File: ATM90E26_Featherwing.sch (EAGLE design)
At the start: 56 parts, among them J1 ST-PJ-312, J2 4P-SMD-2.0-90D, J3 4P-SMD-2.0-90D, J4 12V AC, Q1 8.192MHz, U1 ATM90E26, U2 CJT1117-5.0-SOT223

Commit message: Applied hackvana DRU
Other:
- note added: "Grove Connectors"
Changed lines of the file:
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@@
 <?xml version="1.0" encoding="utf-8"?>
 <!DOCTYPE eagle SYSTEM "eagle.dtd">
-<eagle version="7.4.0">
+<eagle version="7.6.0">
 <drawing>
 <settings>
@@
 <grid distance="0.1" unitdist="inch" unit="inch" style="lines" multiple="1" display="no" altdistance="0.01" altunitdist="inch" altunit="inch"/>
 <layers>
-<layer number="1" name="Top" color="4" fill="1" visible="yes" active="no"/>
-<layer number="16" name="Bottom" color="1" fill="1" visible="yes" active="no"/>
-<layer number="17" name="Pads" color="2" fill="1" visible="yes" active="no"/>
-<layer number="18" name="Vias" color="2" fill="1" visible="yes" active="no"/>
-<layer number="19" name="Unrouted" color="6" fill="1" visible="yes" active="no"/>
-<layer number="20" name="Dimension" color="15" fill="1" visible="yes" active="no"/>
-<layer number="21" name="tPlace" color="7" fill="1" visible="yes" active="no"/>
-<layer number="22" name="bPlace" color="13" fill="1" visible="yes" active="no"/>
-<layer number="23" name="tOrigins" color="15" fill="1" visible="yes" active="no"/>
-<layer number="24" name="bOrigins" color="15" fill="1" visible="yes" active="no"/>
-<layer number="25" name="tNames" color="7" fill="1" visible="yes" active="no"/>
-<layer number="26" name="bNames" color="13" fill="1" visible="yes" active="no"/>
-<layer number="27" name="tValues" color="7" fill="1" visible="yes" active="no"/>
-<layer number="28" name="bValues" color="7" fill="1" visible="yes" active="no"/>
+<layer number="1" name="Top" color="4" fill="1" visible="no" active="no"/>
+<layer number="16" name="Bottom" color="1" fill="1" visible="no" active="no"/>
+<layer number="17" name="Pads" color="2" fill="1" visible="no" active="no"/>
+<layer number="18" name="Vias" color="2" fill="1" visible="no" active="no"/>
+<layer number="19" name="Unrouted" color="6" fill="1" visible="no" active="no"/>
+<layer number="20" name="Dimension" color="15" fill="1" visible="no" active="no"/>
+<layer number="21" name="tPlace" color="7" fill="1" visible="no" active="no"/>
+<layer number="22" name="bPlace" color="13" fill="1" visible="no" active="no"/>
+<layer number="23" name="tOrigins" color="15" fill="1" visible="no" active="no"/>
+<layer number="24" name="bOrigins" color="15" fill="1" visible="no" active="no"/>
+<layer number="25" name="tNames" color="7" fill="1" visible="no" active="no"/>
+<layer number="26" name="bNames" color="13" fill="1" visible="no" active="no"/>
+<layer number="27" name="tValues" color="7" fill="1" visible="no" active="no"/>
+<layer number="28" name="bValues" color="7" fill="1" visible="no" active="no"/>
 <layer number="29" name="tStop" color="7" fill="3" visible="no" active="no"/>
 <layer number="30" name="bStop" color="7" fill="6" visible="no" active="no"/>
@@
 <layer number="35" name="tGlue" color="7" fill="4" visible="no" active="no"/>
 <layer number="36" name="bGlue" color="7" fill="5" visible="no" active="no"/>
-<layer number="37" name="tTest" color="7" fill="1" visible="yes" active="no"/>
-<layer number="38" name="bTest" color="7" fill="1" visible="yes" active="no"/>
+<layer number="37" name="tTest" color="7" fill="1" visible="no" active="no"/>
+<layer number="38" name="bTest" color="7" fill="1" visible="no" active="no"/>
 <layer number="39" name="tKeepout" color="4" fill="11" visible="no" active="no"/>
 <layer number="40" name="bKeepout" color="1" fill="11" visible="no" active="no"/>
@@
 <layer number="44" name="Drills" color="7" fill="1" visible="no" active="no"/>
 <layer number="45" name="Holes" color="7" fill="1" visible="no" active="no"/>
-<layer number="46" name="Milling" color="3" fill="1" visible="yes" active="no"/>
-<layer number="47" name="Measures" color="7" fill="1" visible="yes" active="no"/>
-<layer number="48" name="Document" color="7" fill="1" visible="yes" active="no"/>
-<layer number="49" name="Reference" color="7" fill="1" visible="yes" active="no"/>
-<layer number="50" name="dxf" color="7" fill="1" visible="yes" active="no"/>
-<layer number="51" name="tDocu" color="7" fill="1" visible="yes" active="no"/>
-<layer number="52" name="bDocu" color="7" fill="1" visible="yes" active="no"/>
-<layer number="53" name="tGND_GNDA" color="7" fill="9" visible="yes" active="no"/>
-<layer number="54" name="bGND_GNDA" color="1" fill="9" visible="yes" active="no"/>
-<layer number="56" name="wert" color="7" fill="1" visible="yes" active="no"/>
-<layer number="57" name="tCAD" color="7" fill="1" visible="yes" active="no"/>
-<layer number="59" name="tCarbon" color="7" fill="1" visible="yes" active="no"/>
-<layer number="60" name="bCarbon" color="7" fill="1" visible="yes" active="no"/>
+<layer number="46" name="Milling" color="3" fill="1" visible="no" active="no"/>
+<layer number="47" name="Measures" color="7" fill="1" visible="no" active="no"/>
+<layer number="48" name="Document" color="7" fill="1" visible="no" active="no"/>
+<layer number="49" name="Reference" color="7" fill="1" visible="no" active="no"/>
+<layer number="50" name="dxf" color="7" fill="1" visible="no" active="no"/>
+<layer number="51" name="tDocu" color="7" fill="1" visible="no" active="no"/>
+<layer number="52" name="bDocu" color="7" fill="1" visible="no" active="no"/>
+<layer number="53" name="tGND_GNDA" color="7" fill="9" visible="no" active="no"/>
+<layer number="54" name="bGND_GNDA" color="1" fill="9" visible="no" active="no"/>
+<layer number="56" name="wert" color="7" fill="1" visible="no" active="no"/>
+<layer number="57" name="tCAD" color="7" fill="1" visible="no" active="no"/>
+<layer number="59" name="tCarbon" color="7" fill="1" visible="no" active="no"/>
+<layer number="60" name="bCarbon" color="7" fill="1" visible="no" active="no"/>
 <layer number="90" name="Modules" color="5" fill="1" visible="yes" active="yes"/>
 <layer number="91" name="Nets" color="2" fill="1" visible="yes" active="yes"/>
@@
 <wire x1="101.6" y1="22.86" x2="101.6" y2="-76.2" width="0.1524" layer="94"/>
 <text x="0" y="17.78" size="2.54" layer="94">Voltage and Current Sampling + Supply</text>
+<text x="142.24" y="-22.86" size="2.54" layer="94">Grove Connectors</text>
 </plain>
 <instances>

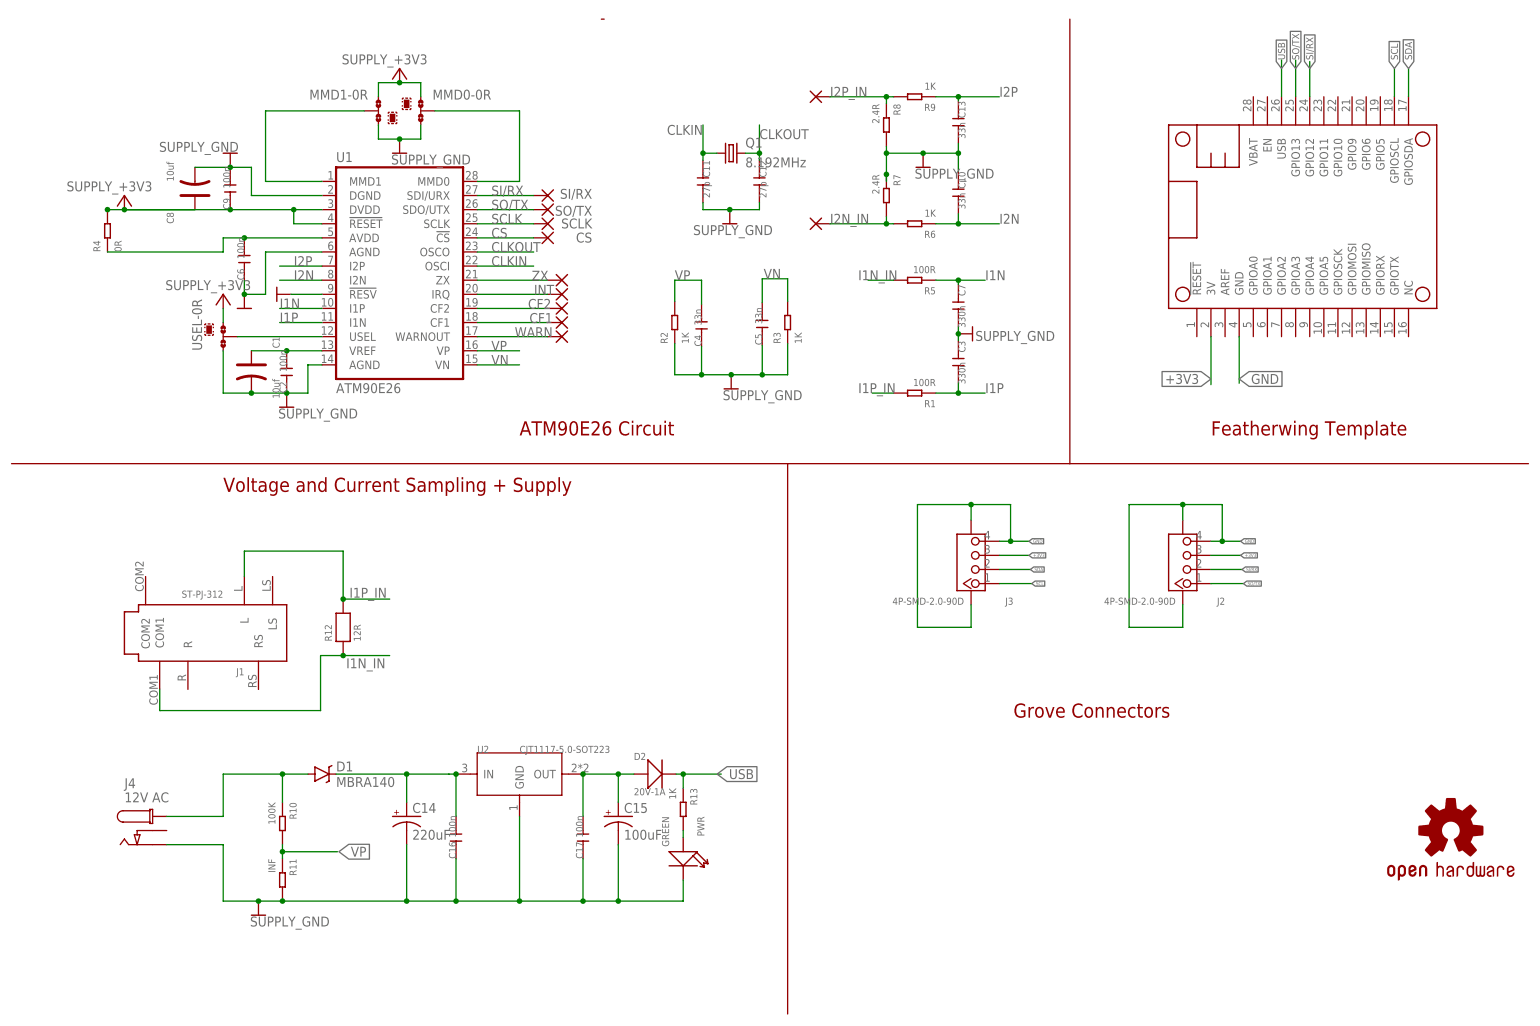
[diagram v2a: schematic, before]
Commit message: Ass spi/uart mux pins
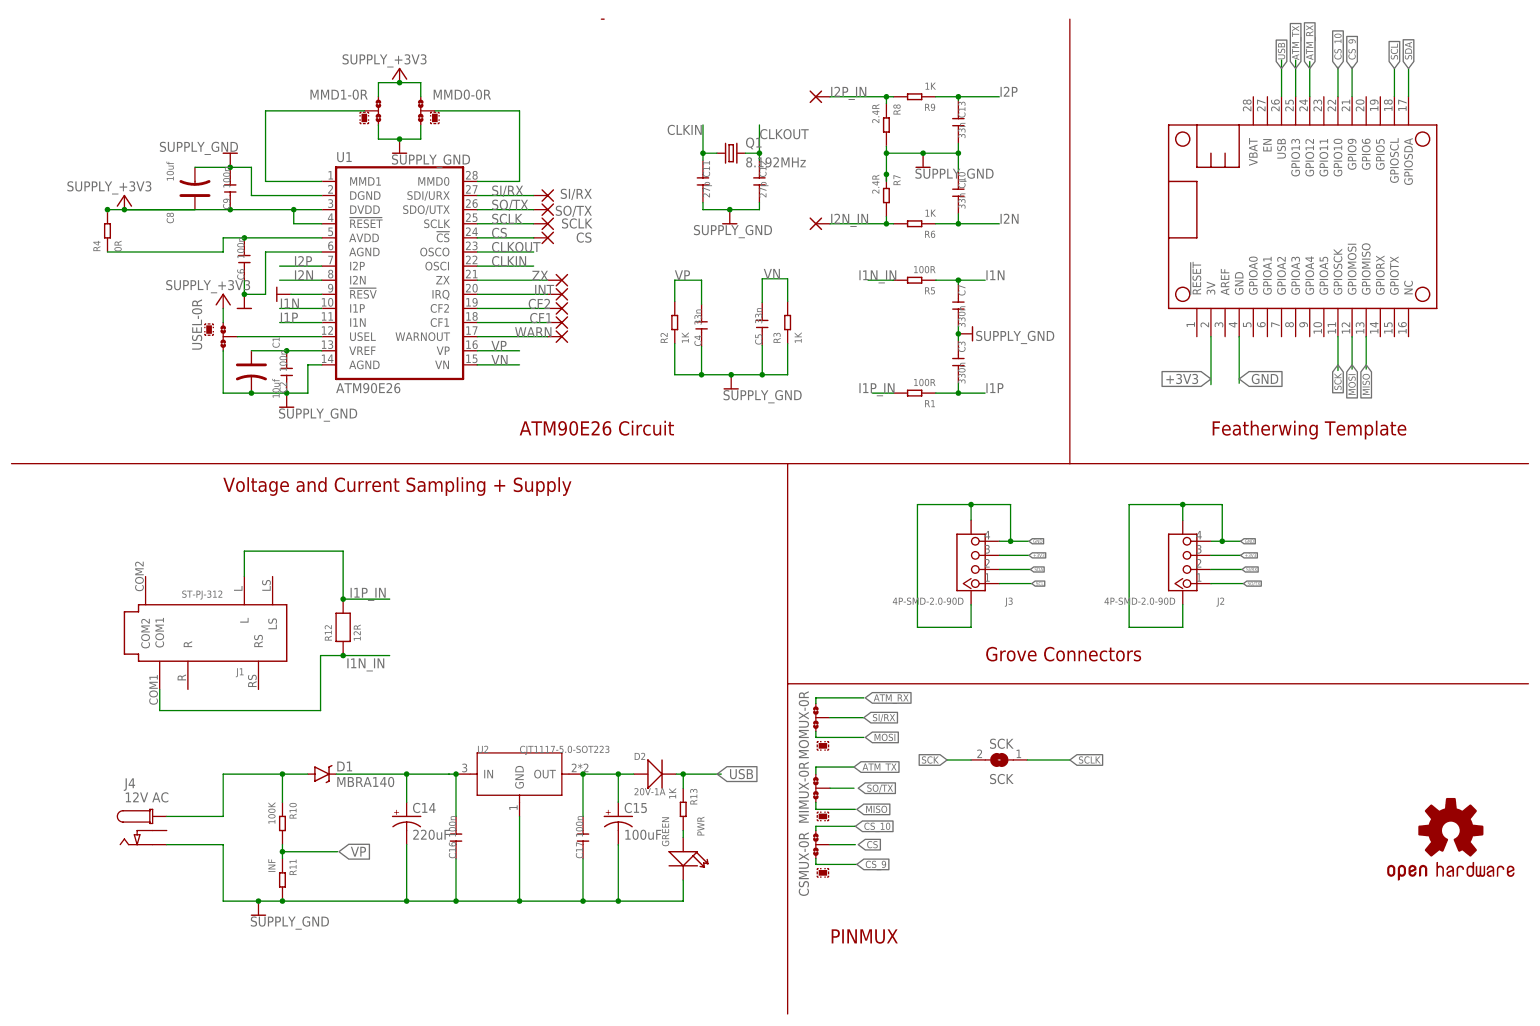
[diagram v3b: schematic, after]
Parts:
- added CSMUX, MIMUX, MOMUX: 0R-JUMPA, jump-0r-smd:0R-JUMPA
- added SCK: SCK, jumper:SJ
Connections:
- new net ATM_RX: MOMUX-0R.1, MS1.GPIO12
- new net ATM_TX: MIMUX-0R.1, MS1.GPIO13
- new net CS_10: CSMUX-0R.1, MS1.GPIO10
- new net CS_9: CSMUX-0R.3, MS1.GPIO9
- new net MISO: MIMUX-0R.3, MS1.GPIOMISO
- new net MOSI: MOMUX-0R.3, MS1.GPIOMOSI
- new net SCK: MS1.GPIOSCK, SCK.2
- net CS: now also CSMUX-0R.2
- net SCLK: now also SCK.1
- net SI/RX: now also MOMUX-0R.2; no longer MS1.GPIO12
- net SO/TX: now also MIMUX-0R.2; no longer MS1.GPIO13
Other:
- note added: "PINMUX"
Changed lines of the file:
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@@
 <?xml version="1.0" encoding="utf-8"?>
 <!DOCTYPE eagle SYSTEM "eagle.dtd">
-<eagle version="7.6.0">
+<eagle version="7.4.0">
 <drawing>
 <settings>
@@
 <layers>
 <layer number="1" name="Top" color="4" fill="1" visible="no" active="no"/>
+<layer number="2" name="Route2" color="1" fill="3" visible="no" active="no"/>
+<layer number="15" name="Route15" color="4" fill="6" visible="no" active="no"/>
 <layer number="16" name="Bottom" color="1" fill="1" visible="no" active="no"/>
 <layer number="17" name="Pads" color="2" fill="1" visible="no" active="no"/>
@@
 <part name="C16" library="Discrete" deviceset="C*" device="-0603" value="100n"/>
 <part name="C17" library="Discrete" deviceset="C*" device="-0603" value="100n"/>
+<part name="MOMUX" library="jump-0r-smd" deviceset="0R-JUMP" device="A" value="0R-JUMPA"/>
+<part name="MIMUX" library="jump-0r-smd" deviceset="0R-JUMP" device="A" value="0R-JUMPA"/>
+<part name="CSMUX" library="jump-0r-smd" deviceset="0R-JUMP" device="A" value="0R-JUMPA"/>
+<part name="SCK" library="jumper" deviceset="SJ" device="" value="SCK"/>
 </parts>
 <sheets>
@@
 <text x="53.34" y="27.94" size="2.54" layer="94" ratio="20">ATM90E26 Circuit</text>
 <text x="177.8" y="27.94" size="2.54" layer="94" ratio="20">Featherwing Template</text>
-<wire x1="101.6" y1="22.86" x2="101.6" y2="-76.2" width="0.1524" layer="94"/>
+<wire x1="101.6" y1="22.86" x2="101.6" y2="-16.764" width="0.1524" layer="94"/>
 <text x="0" y="17.78" size="2.54" layer="94">Voltage and Current Sampling + Supply</text>
-<text x="142.24" y="-22.86" size="2.54" layer="94">Grove Connectors</text>
+<text x="137.16" y="-12.7" size="2.54" layer="94">Grove Connectors</text>
+<wire x1="101.6" y1="-16.764" x2="101.6" y2="-76.2" width="0.1524" layer="94"/>
+<wire x1="101.6" y1="-16.764" x2="234.95" y2="-16.764" width="0.1524" layer="94"/>
+<text x="109.22" y="-63.5" size="2.54" layer="94">PINMUX</text>
 </plain>
 <instances>
@@
 <attribute name="NAME" x="15.494" y="88.392" size="1.778" layer="95"/>
 </instance>
-<instance part="MMD1" gate="G$2" x="30.48" y="83.82" rot="R180"/>
+<instance part="MMD1" gate="G$2" x="25.4" y="83.82" rot="R180"/>
 <instance part="MMD0" gate="-0R" x="35.56" y="86.36" smashed="yes">
 <attribute name="NAME" x="48.26" y="90.17" size="1.778" layer="95" rot="R180"/>
 </instance>
-<instance part="MMD0" gate="G$2" x="33.02" y="88.9"/>
+<instance part="MMD0" gate="G$2" x="38.1" y="83.82" rot="R180"/>
 <instance part="+3V3" gate="G$1" x="31.75" y="91.44" smashed="yes">
 <attribute name="VALUE" x="21.336" y="94.742" size="1.778" layer="96"/>
@@
 <instance part="C16" gate="C" x="41.91" y="-44.45" rot="R90"/>
 <instance part="C17" gate="C" x="64.77" y="-44.45" rot="R90"/>
+<instance part="MOMUX" gate="-0R" x="106.68" y="-22.86" smashed="yes">
+<attribute name="NAME" x="103.632" y="-18.034" size="1.778" layer="95" rot="R270"/>
+</instance>
+<instance part="MOMUX" gate="G$2" x="109.22" y="-27.94" rot="R270"/>
+<instance part="MIMUX" gate="-0R" x="106.68" y="-35.56" smashed="yes">
+<attribute name="NAME" x="103.632" y="-30.734" size="1.778" layer="95" rot="R270"/>
+</instance>
+<instance part="MIMUX" gate="G$2" x="109.22" y="-40.64" rot="R270"/>
+<instance part="CSMUX" gate="-0R" x="106.68" y="-45.72" smashed="yes">
+<attribute name="NAME" x="103.632" y="-43.434" size="1.778" layer="95" rot="R270"/>
+</instance>
+<instance part="CSMUX" gate="G$2" x="109.22" y="-50.8" rot="R270"/>
+<instance part="SCK" gate="1" x="139.7" y="-30.48" rot="R180"/>
 </instances>
 <busses>
@@
 <pinref part="CS" gate="G$1" pin="P"/>
 </segment>
+<segment>
+<pinref part="CSMUX" gate="-0R" pin="2"/>
+<wire x1="109.22" y1="-45.72" x2="113.792" y2="-45.72" width="0.1524" layer="91"/>
+<label x="114.3" y="-45.72" size="1.27" layer="95" xref="yes"/>
+</segment>
 </net>
 <net name="SCLK" class="0">
@@
 <label x="48.26" y="66.04" size="1.778" layer="95"/>
 <pinref part="SCLK" gate="G$1" pin="P"/>
+</segment>
+<segment>
+<pinref part="SCK" gate="1" pin="1"/>
+<wire x1="144.78" y1="-30.48" x2="152.4" y2="-30.48" width="0.1524" layer="91"/>
+<label x="152.4" y="-30.48" size="1.27" layer="95" xref="yes"/>
 </segment>
 </net>
@@
 </segment>
 <segment>
-<pinref part="MS1" gate="G$1" pin="GPIO12"/>
-<wire x1="195.58" y1="88.9" x2="195.58" y2="95.25" width="0.1524" layer="91"/>
-<label x="195.58" y="93.98" size="1.27" layer="95" rot="R90" xref="yes"/>
+<pinref part="MOMUX" gate="-0R" pin="2"/>
+<wire x1="109.22" y1="-22.86" x2="115.316" y2="-22.86" width="0.1524" layer="91"/>
+<label x="115.316" y="-22.86" size="1.27" layer="95" xref="yes"/>
 </segment>
 </net>
@@
 </segment>
 <segment>
-<pinref part="MS1" gate="G$1" pin="GPIO13"/>
-<wire x1="193.04" y1="88.9" x2="193.04" y2="95.504" width="0.1524" layer="91"/>
-<label x="193.04" y="93.98" size="1.27" layer="95" rot="R90" xref="yes"/>
+<pinref part="MIMUX" gate="-0R" pin="2"/>
+<wire x1="109.22" y1="-35.56" x2="113.538" y2="-35.56" width="0.1524" layer="91"/>
+<label x="114.3" y="-35.56" size="1.27" layer="95" xref="yes"/>
 </segment>
 </net>
@@
 </segment>
 </net>
+<net name="SCK" class="0">
+<segment>
+<pinref part="MS1" gate="G$1" pin="GPIOSCK"/>
+<wire x1="200.66" y1="45.72" x2="200.66" y2="39.624" width="0.1524" layer="91"/>
+<label x="200.66" y="40.64" size="1.27" layer="95" rot="R270" xref="yes"/>
+</segment>
+<segment>
+<pinref part="SCK" gate="1" pin="2"/>
+<wire x1="134.62" y1="-30.48" x2="130.302" y2="-30.48" width="0.1524" layer="91"/>
+<label x="130.302" y="-30.48" size="1.27" layer="95" rot="R180" xref="yes"/>
+</segment>
+</net>
+<net name="MOSI" class="0">
+<segment>
+<pinref part="MS1" gate="G$1" pin="GPIOMOSI"/>
+<wire x1="203.2" y1="45.72" x2="203.2" y2="39.878" width="0.1524" layer="91"/>
+<label x="203.2" y="40.64" size="1.27" layer="95" rot="R270" xref="yes"/>
+</segment>
+<segment>
+<pinref part="MOMUX" gate="-0R" pin="3"/>
+<wire x1="106.68" y1="-25.4" x2="106.68" y2="-26.416" width="0.1524" layer="91"/>
+<wire x1="106.68" y1="-26.416" x2="115.316" y2="-26.416" width="0.1524" layer="91"/>
+<label x="115.57" y="-26.416" size="1.27" layer="95" xref="yes"/>
+</segment>
+</net>
+<net name="MISO" class="0">
+<segment>
+<pinref part="MS1" gate="G$1" pin="GPIOMISO"/>
+<wire x1="205.74" y1="45.72" x2="205.74" y2="39.878" width="0.1524" layer="91"/>
+<label x="205.74" y="40.64" size="1.27" layer="95" rot="R270" xref="yes"/>
+</segment>
+<segment>
+<pinref part="MIMUX" gate="-0R" pin="3"/>
+<wire x1="106.68" y1="-38.1" x2="106.68" y2="-39.37" width="0.1524" layer="91"/>
+<wire x1="106.68" y1="-39.37" x2="113.792" y2="-39.37" width="0.1524" layer="91"/>
+<label x="114.046" y="-39.37" size="1.27" layer="95" xref="yes"/>
+</segment>
+</net>
+<net name="CS_10" class="0">
+<segment>
+<pinref part="MS1" gate="G$1" pin="GPIO10"/>
+<wire x1="200.66" y1="88.9" x2="200.66" y2="94.234" width="0.1524" layer="91"/>
+<label x="200.66" y="93.98" size="1.27" layer="95" rot="R90" xref="yes"/>
+</segment>
+<segment>
+<pinref part="CSMUX" gate="-0R" pin="1"/>
+<wire x1="106.68" y1="-43.18" x2="106.68" y2="-42.418" width="0.1524" layer="91"/>
+<wire x1="106.68" y1="-42.418" x2="113.792" y2="-42.418" width="0.1524" layer="91"/>
+<label x="113.792" y="-42.418" size="1.27" layer="95" xref="yes"/>
+</segment>
+</net>
+<net name="CS_9" class="0">
+<segment>
+<pinref part="MS1" gate="G$1" pin="GPIO9"/>
+<wire x1="203.2" y1="88.9" x2="203.2" y2="94.234" width="0.1524" layer="91"/>
+<label x="203.2" y="93.98" size="1.27" layer="95" rot="R90" xref="yes"/>
+</segment>
+<segment>
+<pinref part="CSMUX" gate="-0R" pin="3"/>
+<wire x1="106.68" y1="-48.26" x2="106.68" y2="-49.276" width="0.1524" layer="91"/>
+<wire x1="106.68" y1="-49.276" x2="114.046" y2="-49.276" width="0.1524" layer="91"/>
+<label x="114.046" y="-49.276" size="1.27" layer="95" xref="yes"/>
+</segment>
+</net>
+<net name="ATM_TX" class="0">
+<segment>
+<pinref part="MS1" gate="G$1" pin="GPIO13"/>
+<wire x1="193.04" y1="88.9" x2="193.04" y2="95.504" width="0.1524" layer="91"/>
+<label x="193.04" y="93.98" size="1.27" layer="95" rot="R90" xref="yes"/>
+</segment>
+<segment>
+<pinref part="MIMUX" gate="-0R" pin="1"/>
+<wire x1="106.68" y1="-33.02" x2="106.68" y2="-31.75" width="0.1524" layer="91"/>
+<wire x1="106.68" y1="-31.75" x2="113.538" y2="-31.75" width="0.1524" layer="91"/>
+<label x="113.538" y="-31.75" size="1.27" layer="95" xref="yes"/>
+</segment>
+</net>
+<net name="ATM_RX" class="0">
+<segment>
+<pinref part="MS1" gate="G$1" pin="GPIO12"/>
+<wire x1="195.58" y1="88.9" x2="195.58" y2="95.25" width="0.1524" layer="91"/>
+<label x="195.58" y="93.98" size="1.27" layer="95" rot="R90" xref="yes"/>
+</segment>
+<segment>
+<pinref part="MOMUX" gate="-0R" pin="1"/>
+<wire x1="106.68" y1="-20.32" x2="106.68" y2="-19.304" width="0.1524" layer="91"/>
+<wire x1="106.68" y1="-19.304" x2="115.316" y2="-19.304" width="0.1524" layer="91"/>
+<label x="115.57" y="-19.304" size="1.27" layer="95" xref="yes"/>
+</segment>
+</net>
